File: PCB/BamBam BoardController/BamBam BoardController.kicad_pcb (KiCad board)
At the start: 2 copper layers, 85.1 x 52.1 mm, 74 parts, among them IC1 CNY74-2, IC2 CNY74-2, P1 BremsOpto, Q1 IRLR2905z, Q2 IRLR2905z, Q3 IRLR2905z, Q4 IRLR2905z, Q5 IRLR2905z, U1 TEENSY_3.1+4, U2 HC_05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

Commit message: Auf BamBam angepasst. HC-05 Rahmen lag auf Pads BrmesOpto Text durch Bremse erstezt Gerber und Drill-Dateien generiert und gesichtet
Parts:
- P1: value BremsOpto -> Bremse
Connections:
- net /TeensyS2/BEC_A-5V renamed /BamBam BoardController/BEC_A-5V
- net /TeensyS2/BEC_B-5V renamed /BamBam BoardController/BEC_B-5V
- net /TeensyS2/Blinker_L_Out renamed /BamBam BoardController/Blinker_L_Out
- net /TeensyS2/Blinker_R_Out renamed /BamBam BoardController/Blinker_R_Out
- net /TeensyS2/Brems_Vcc renamed /BamBam BoardController/Brems_Vcc
- net /TeensyS2/Bremse_Out renamed /BamBam BoardController/Bremse_Out
- net /TeensyS2/GND_BEC_A renamed /BamBam BoardController/GND_BEC_A
- net /TeensyS2/GND_BEC_B renamed /BamBam BoardController/GND_BEC_B
- net /TeensyS2/Hupe_Out renamed /BamBam BoardController/Hupe_Out
- net /TeensyS2/Licht_Out renamed /BamBam BoardController/Licht_Out
- net /TeensyS2/Motor_Opto_A renamed /BamBam BoardController/Motor_Opto_A
- net /TeensyS2/Motor_Opto_B renamed /BamBam BoardController/Motor_Opto_B

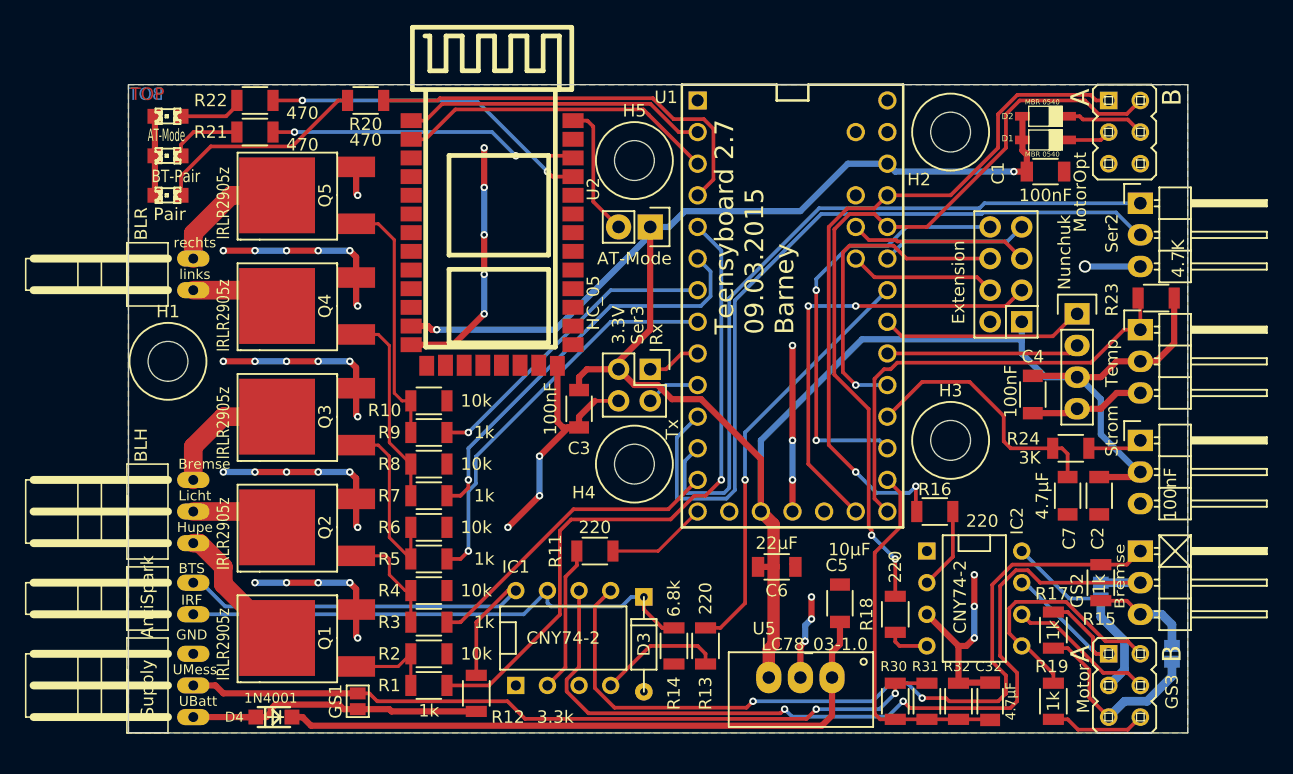
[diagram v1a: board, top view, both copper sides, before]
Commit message: Bohrungen für die PC352 und PC353, sowie für die Motorstiftleisten auf 0.965 bzw. 1.0mm vergrößert. Zwei Leiterbahnen wegen Kollisionsmöglichkeit verschoben. Text auf Leiterplatte auf BamBam und Datum angepasst. Gerber-Dateien und Borhdaten überprüft.
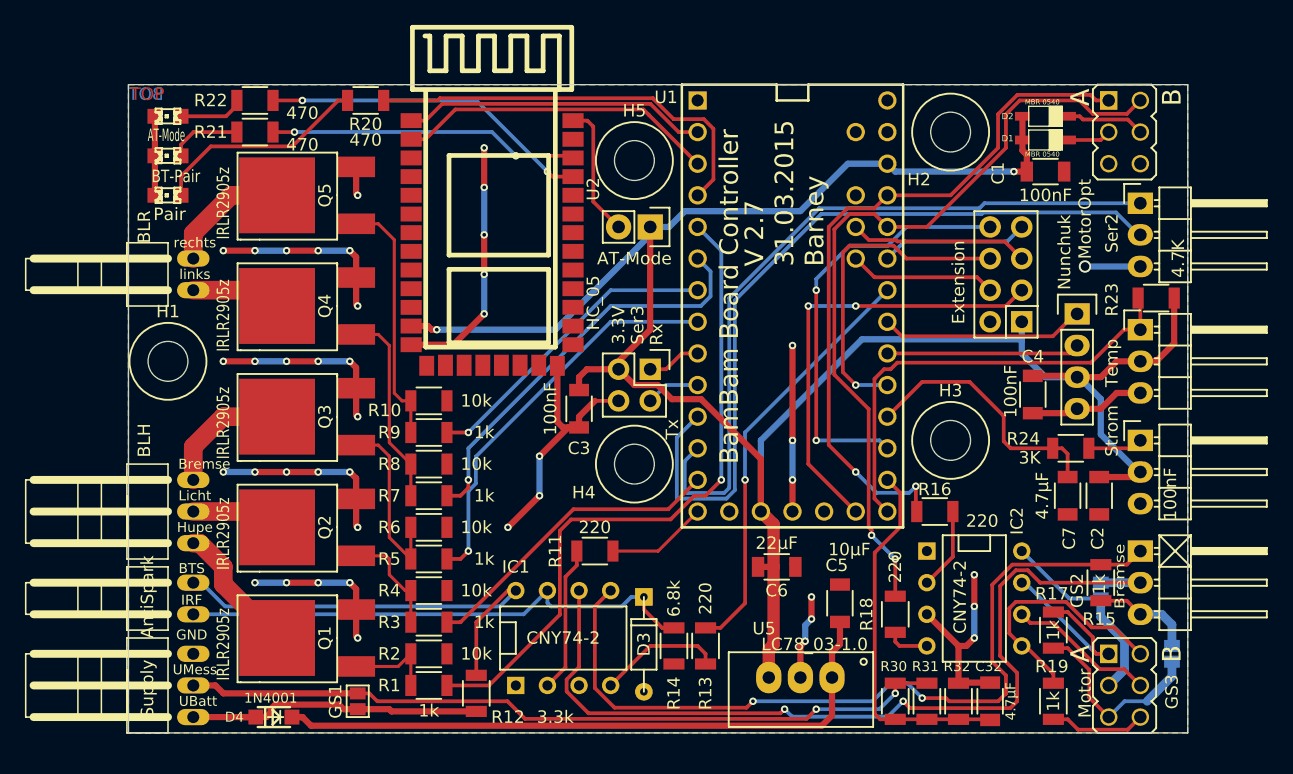
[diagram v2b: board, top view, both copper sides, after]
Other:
- board text added: "BamBam Board Controller"
- board text added: "V 2.7 31.03.2015 Barney"
- board text removed: "Teensyboard 2.7 09.03.2015 Barney"

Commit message: Anpassung an die KiCAD Libs >02/2015 Einige kleine Korrekturen am Layout Anpassung der Mounting Holes mit NTPH (nicht durch kontaktieren) Zwei Texte im PCB zugefügt (Tx und Rx Ser2)
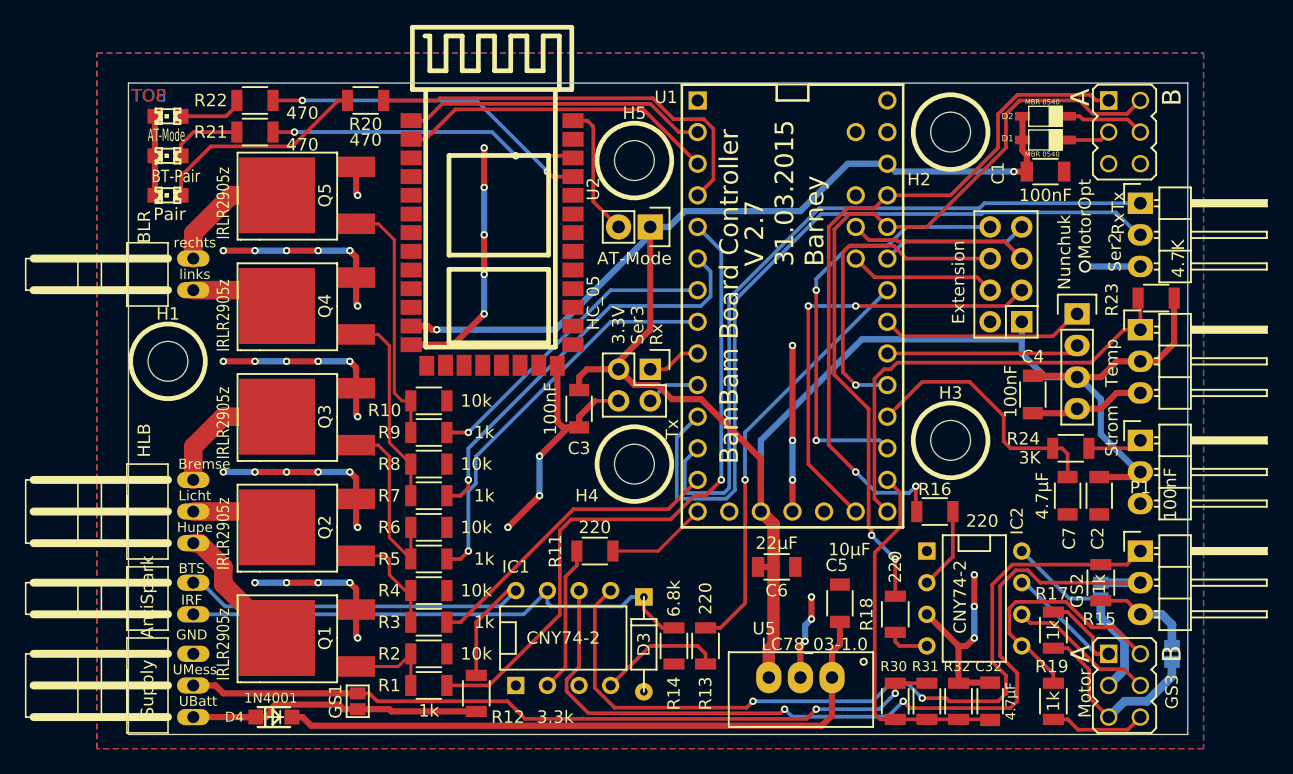
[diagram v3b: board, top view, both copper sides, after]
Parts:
- H1, H2, H3, H4, H5: footprint packages:MountingHole_3mm_new -> packages:MountingHole_3mm
- X2: value BLH -> HLB
- moved P1 2.54 mm to (170.2, 111.1), turned to 0 degrees
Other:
- board size 85.1 x 52.1 mm -> 85.1 x 52.3 mm

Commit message: Files komplett mit aktuellen Dateien aus Barneys zip-Archiv überschrieben.
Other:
- board text added: "3V3"
- board text added: "A1"
- board text added: "A10"
- board text added: "A11"
- board text added: "A14"
- board text added: "A3"
- board text added: "A7"
- board text added: "Data"
- board text added: "V 2.71 17.04.2015 Barney"
- board text removed: "V 2.7 31.03.2015 Barney"
